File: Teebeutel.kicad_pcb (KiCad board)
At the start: 2 copper layers, 72 x 100 mm, 130 parts, among them J1 RJ45_Shielded, J2 Micro_SD_Card, J3 Battery, J4 Conn_01x30_Female, Q1 S8050, Q2 S8050, SW1 K1-1506SN-01, SW2 SW_SPST, U1 LIS2DE12, U10 TLV1117-33, U2 ESP32-WROOM-32, U3 TXB0104RUT, U4 TXB0104RUT, U5 SGP30, U6 PPSI262, U7 MCP73831-2-OT, U8 TLV70018_SOT23-5, U9 SDB628

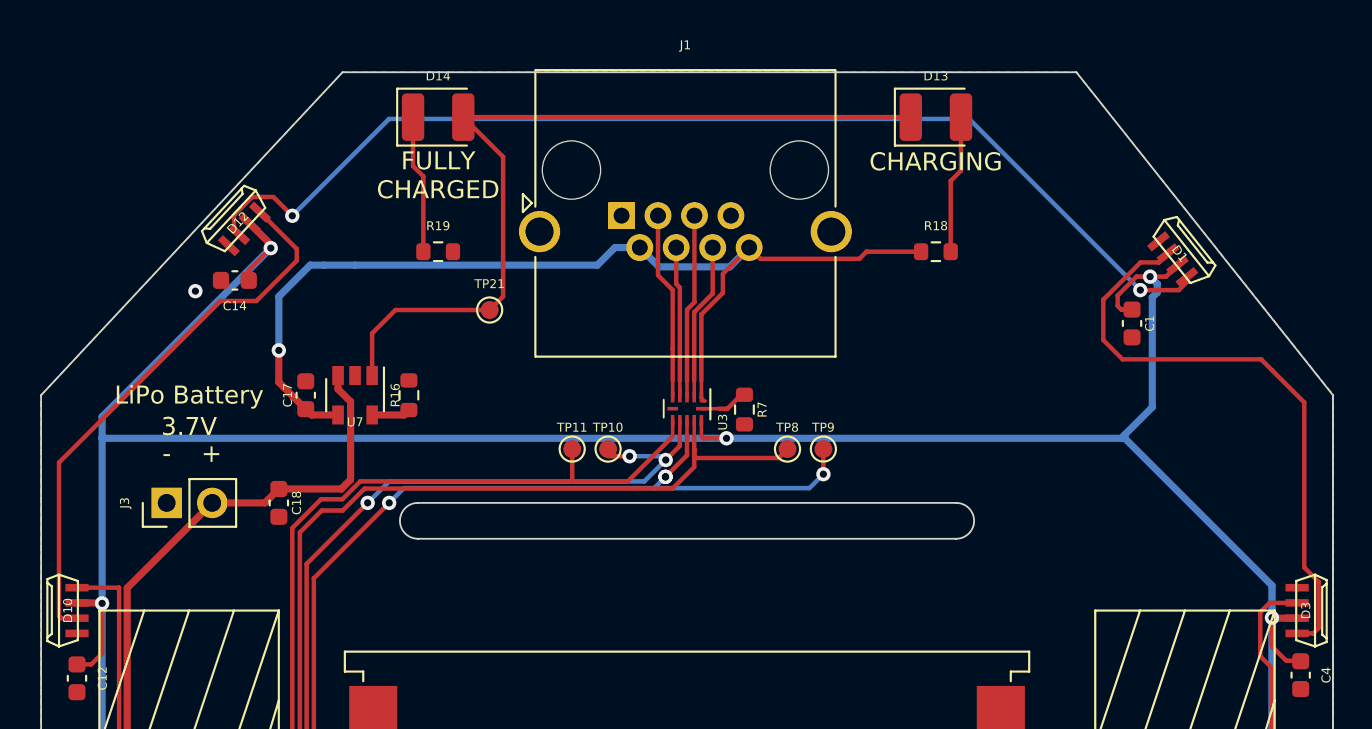
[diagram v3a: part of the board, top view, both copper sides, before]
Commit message: feat(): finish routing and assigning JLCPCB part numbers
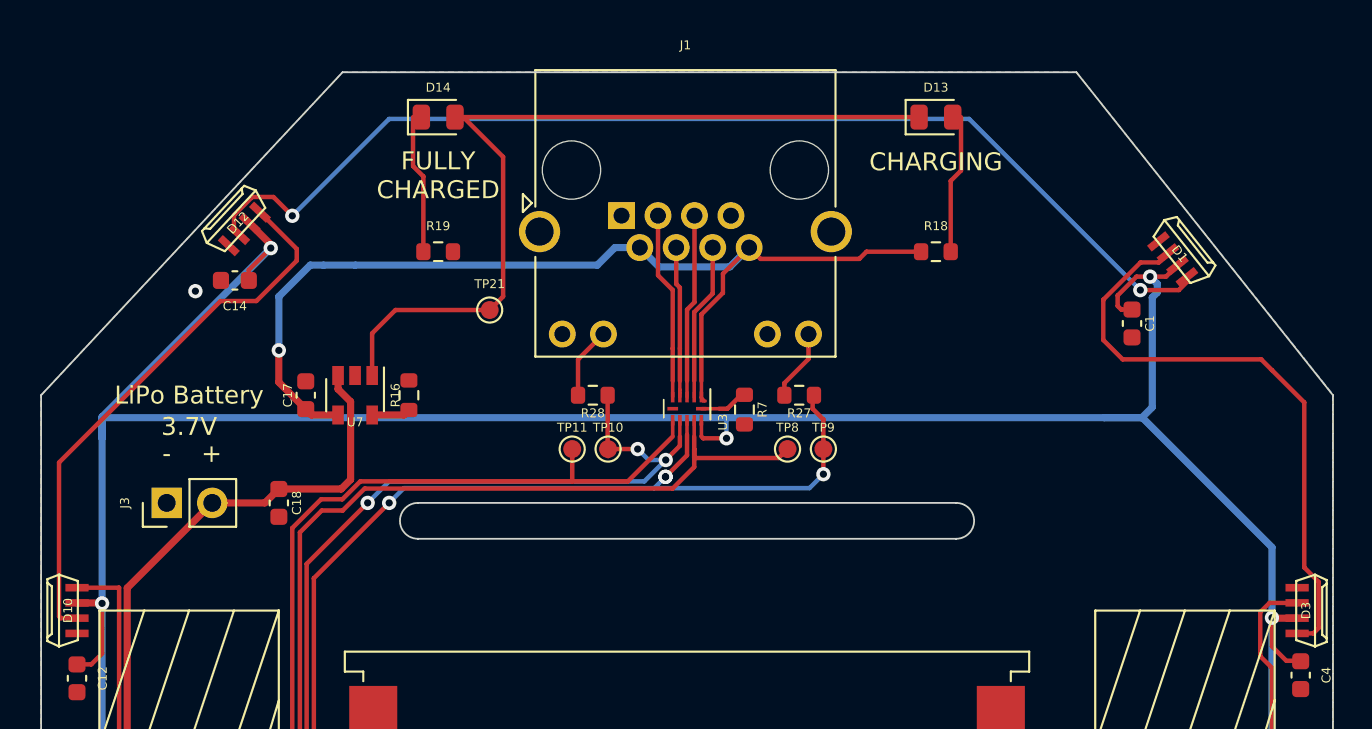
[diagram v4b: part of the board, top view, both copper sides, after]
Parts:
- added R27: 100, Resistor_SMD:R_0603_1608Metric, F.Cu at (152.2, 68.0)
- added R28: 100, Resistor_SMD:R_0603_1608Metric, F.Cu at (140.8, 68.0)
- D13, D14: footprint LED_SMD:LED_1210_3225Metric -> LED_SMD:LED_0805_2012Metric
- J1: footprint Connector_RJ:RJ45_Amphenol_RJHSE5380 -> Connector_RJ:RJ45_Amphenol_RJHSE538X
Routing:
- net Net-(J1-Pad10): track 0.00 -> 4.00 mm
- net Net-(J1-Pad12): track 0.00 -> 3.97 mm
- net +3V3: track 545.5 -> 549.3 mm
- net RxD: track 104.5 -> 107.8 mm
- net TxD: track 107.5 -> 110.9 mm

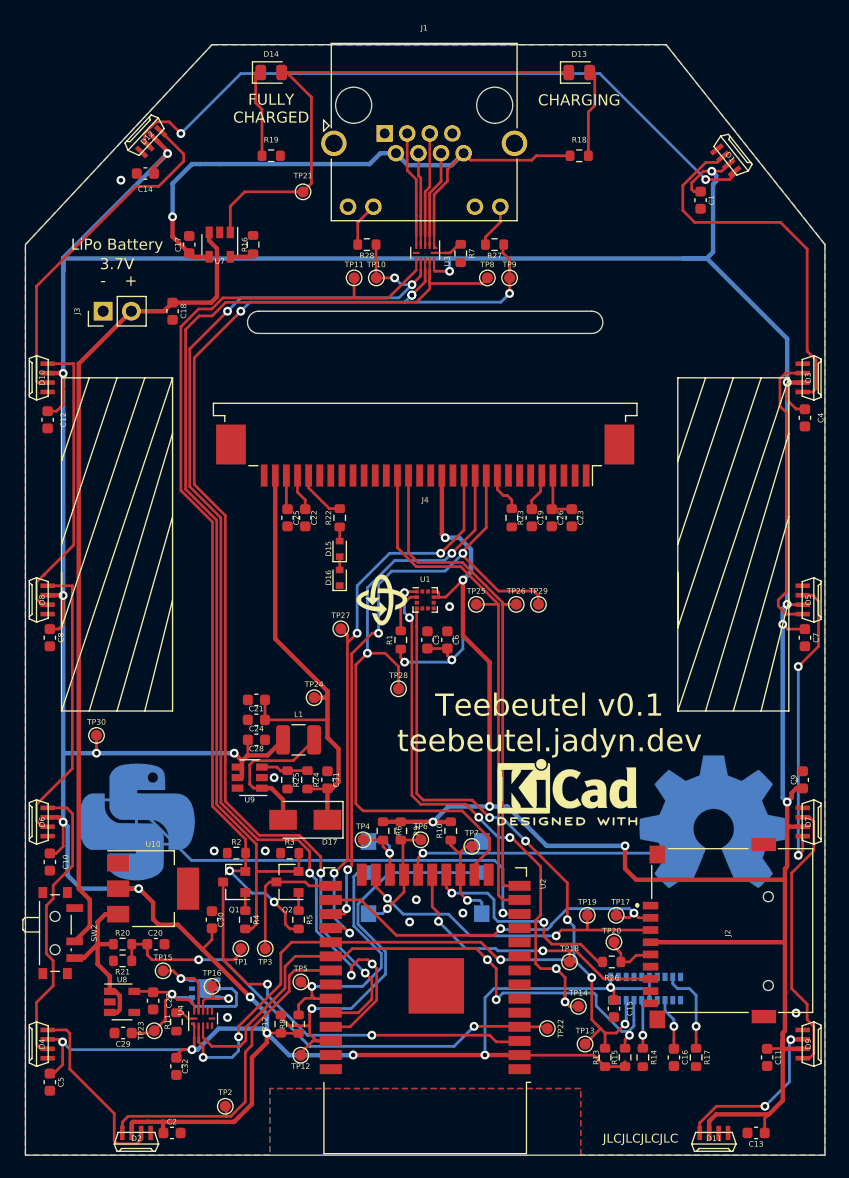
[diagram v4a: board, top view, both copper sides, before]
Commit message: feat(): add IR-Tranceiver and some 3D-Models
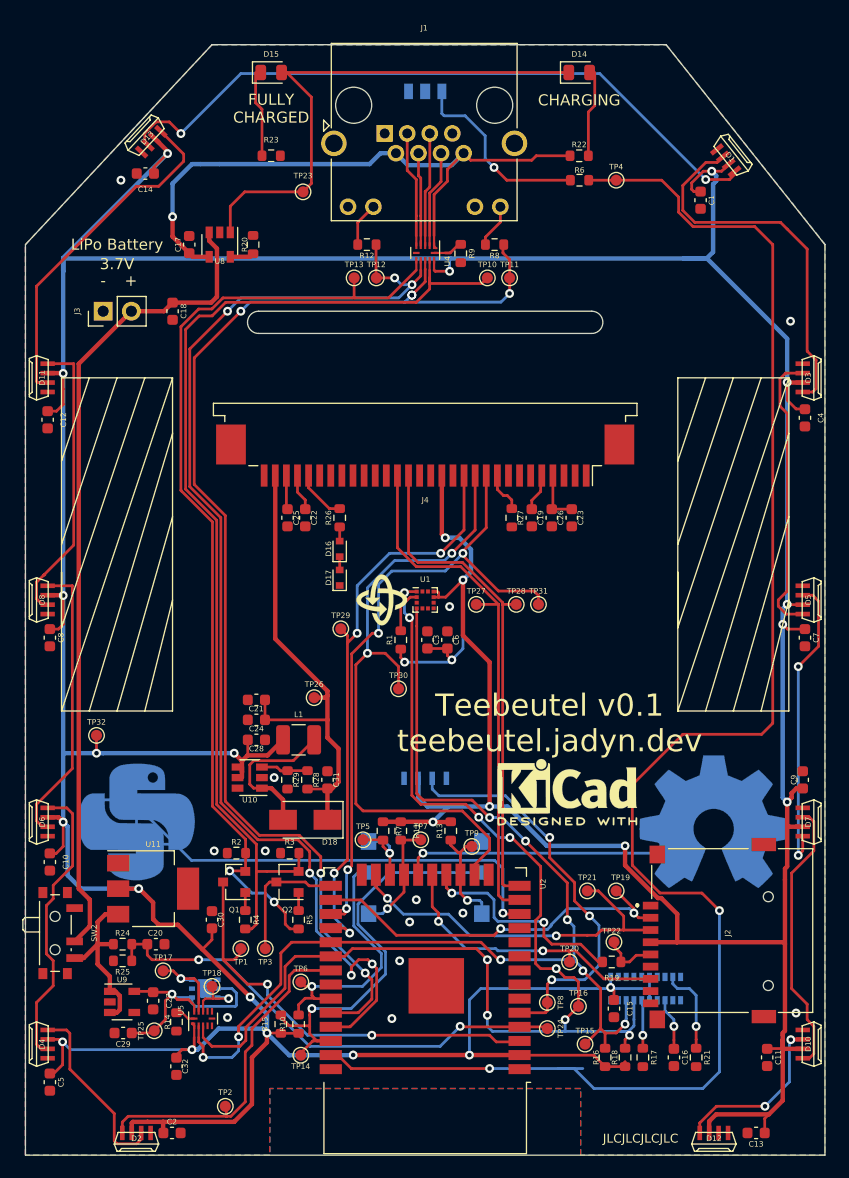
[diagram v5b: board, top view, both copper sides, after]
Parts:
- added D9: LED-IR, Teebeutel_Special_Parts:LKIR30102C, B.Cu at (146.0, 53.8)
- added G***: LOGO, Teebeutel_Graphics:exchange-alt, B.Cu at (146.0, 113.3)
- added G***: LOGO, Teebeutel_Graphics:angle-double-up, B.Cu at (146.0, 64.8)
- added R6: 82, Resistor_SMD:R_0603_1608Metric, F.Cu at (159.9, 62.2)
- added TP4: IR-TX, TestPoint:TestPoint_Pad_D1.0mm, F.Cu at (163.2, 62.2)
- added TP8: IR-RX, TestPoint:TestPoint_Pad_D1.0mm, F.Cu at (157.0, 136.2)
- added U3: RM-V8xxC_TR1, Teebeutel_Special_Parts:IRM-V8xxC-TR1, B.Cu at (146.0, 117.0)
- R26: renamed from R22; value 50 -> 56
- TP17: renamed from TP15; value TestPoint -> I²C SDA 1.8V
- TP18: renamed from TP16; value TestPoint -> I²C SCL 1.8V
- moved TP19 2.20 mm to (163.2, 126.2)
- moved TP21 2.20 mm to (160.6, 126.2)
- renumbered D9 to D10, D10 to D11, D11 to D12, D12 to D13, D13 to D14, D14 to D15, D15 to D16, D16 to D17, D17 to D18, R8 to R10, R9 to R11, R28 to R12, R10 to R13, R11 to R14, R12 to R15, R13 to R16, R14 to R17, R15 to R18, R26 to R19, R16 to R20, R17 to R21, R18 to R22, R19 to R23, R20 to R24, R21 to R25, R23 to R27, R24 to R28, R25 to R29, R6 to R7, R27 to R8, R7 to R9, TP8 to TP10, TP9 to TP11, TP10 to TP12, TP11 to TP13, TP12 to TP14, TP13 to TP15, TP14 to TP16, TP17 to TP19, TP18 to TP20, TP19 to TP21, TP20 to TP22, TP21 to TP23, TP22 to TP24, TP23 to TP25, TP24 to TP26, TP25 to TP27, TP26 to TP28, TP27 to TP29, TP28 to TP30, TP29 to TP31, TP30 to TP32, TP4 to TP5, TP5 to TP6, TP6 to TP7, TP7 to TP9, U9 to U10, U10 to U11, U3 to U4, U4 to U5, U5 to U6, U6 to U7, U7 to U8, U8 to U9
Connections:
- U2 pad 37: (no net) -> IR-TX
- U2 pad 5: (no net) -> IR-RX
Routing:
- net IR-TX: track 0.00 -> 148.8 mm, vias 0 -> 2
- net IR-RX: track 0.00 -> 37.3 mm, vias 0 -> 3
- net Net-(D9-Pad2): track 0.00 -> 17.3 mm, vias 0 -> 1
- net SD-MOSI: track 29.1 -> 33.4 mm
- net I2C-SCL: track 106.2 -> 109.9 mm
- net SD-CS: track 33.1 -> 34.2 mm
- net GND: vias 9 -> 12
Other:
- board text added: "IR"

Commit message: feat(): all 3D-Models are in
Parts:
- added G***: LOGO, Teebeutel_Graphics:bluetooth-b, B.Cu at (137.0, 146.8)
- added G***: LOGO, Teebeutel_Graphics:wifi, B.Cu at (155.0, 146.8)
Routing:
- net +3V3: track 549.3 -> 553.1 mm

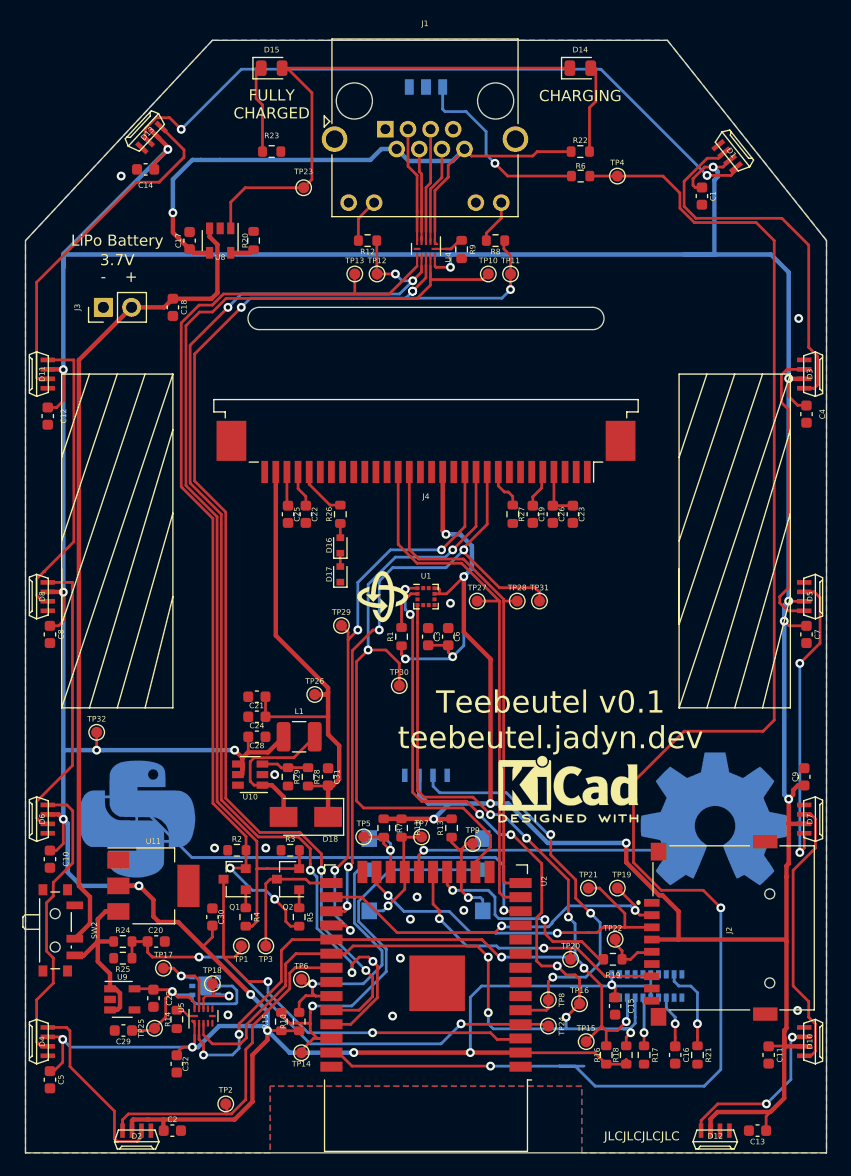
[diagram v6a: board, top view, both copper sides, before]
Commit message: fix: rearanged some traces and vias for better GND planes
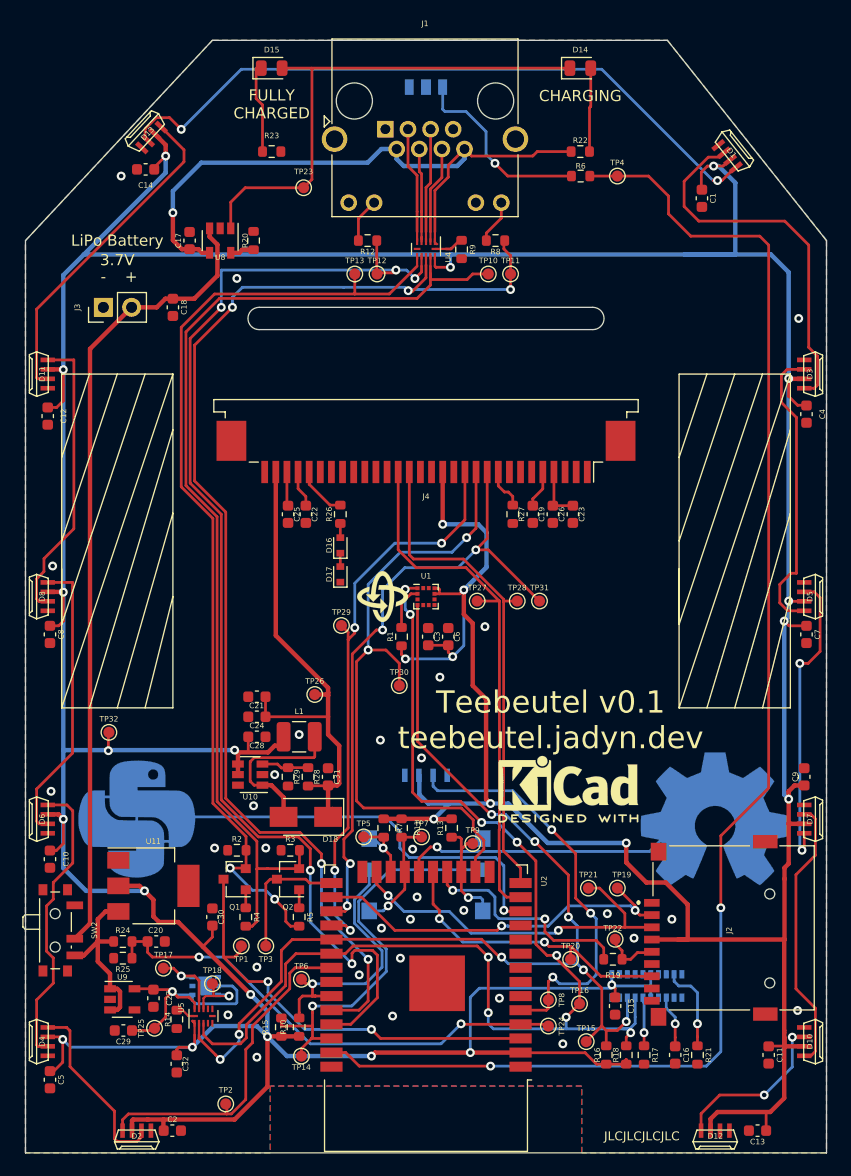
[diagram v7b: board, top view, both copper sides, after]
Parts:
- moved G*** 1.40 mm to (146.0, 63.4)
- moved TP32 1.10 mm to (117.5, 112.2)
- moved R10 0.50 mm to (134.6, 138.7)
- moved R15 0.50 mm to (133.0, 138.7)
- moved TP14 0.30 mm to (134.8, 141.3)
- moved C1 0.20 mm to (170.8, 64.2)
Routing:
- net IR-TX: track 148.8 -> 130.5 mm
- net I2C-SDA: track 100.5 -> 98.0 mm
- net Net-(C18-Pad1): track 74.0 -> 72.3 mm
- net TOUCH9: track 40.9 -> 39.3 mm
- net +3V3: track 553.1 -> 554.6 mm
- net I2C-SCL: track 109.9 -> 108.5 mm
- net RxD: track 107.8 -> 109.0 mm, vias 6 -> 5
- net OLED-RES: track 59.0 -> 57.8 mm
- net +5V: track 56.8 -> 58.0 mm
- net Net-(D11-Pad3): track 31.1 -> 29.9 mm
- net BTN_DOWN: track 7.88 -> 6.83 mm
- net Net-(D18-Pad2): track 13.5 -> 14.5 mm
- net BTN_RIGHT: track 38.5 -> 37.5 mm
- net IR-RX: track 37.3 -> 38.2 mm
- net Net-(D3-Pad3): track 25.8 -> 26.7 mm
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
